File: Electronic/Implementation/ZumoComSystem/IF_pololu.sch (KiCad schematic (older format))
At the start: 38 parts, among them J4 Left, J5 Conn_02x07_Odd_Even, J6 Right, J7 Conn_02x07_Odd_Even, Q10 SI2302CDS-T1-BE3, Q6 SI2302CDS-T1-BE3, Q7 SI2302CDS-T1-BE3, Q8 SI2302CDS-T1-BE3, Q9 SI2302CDS-T1-BE3, SW3 KMR221GLFS, SW4 KMR221GLFS, SW5 KMR221GLFS

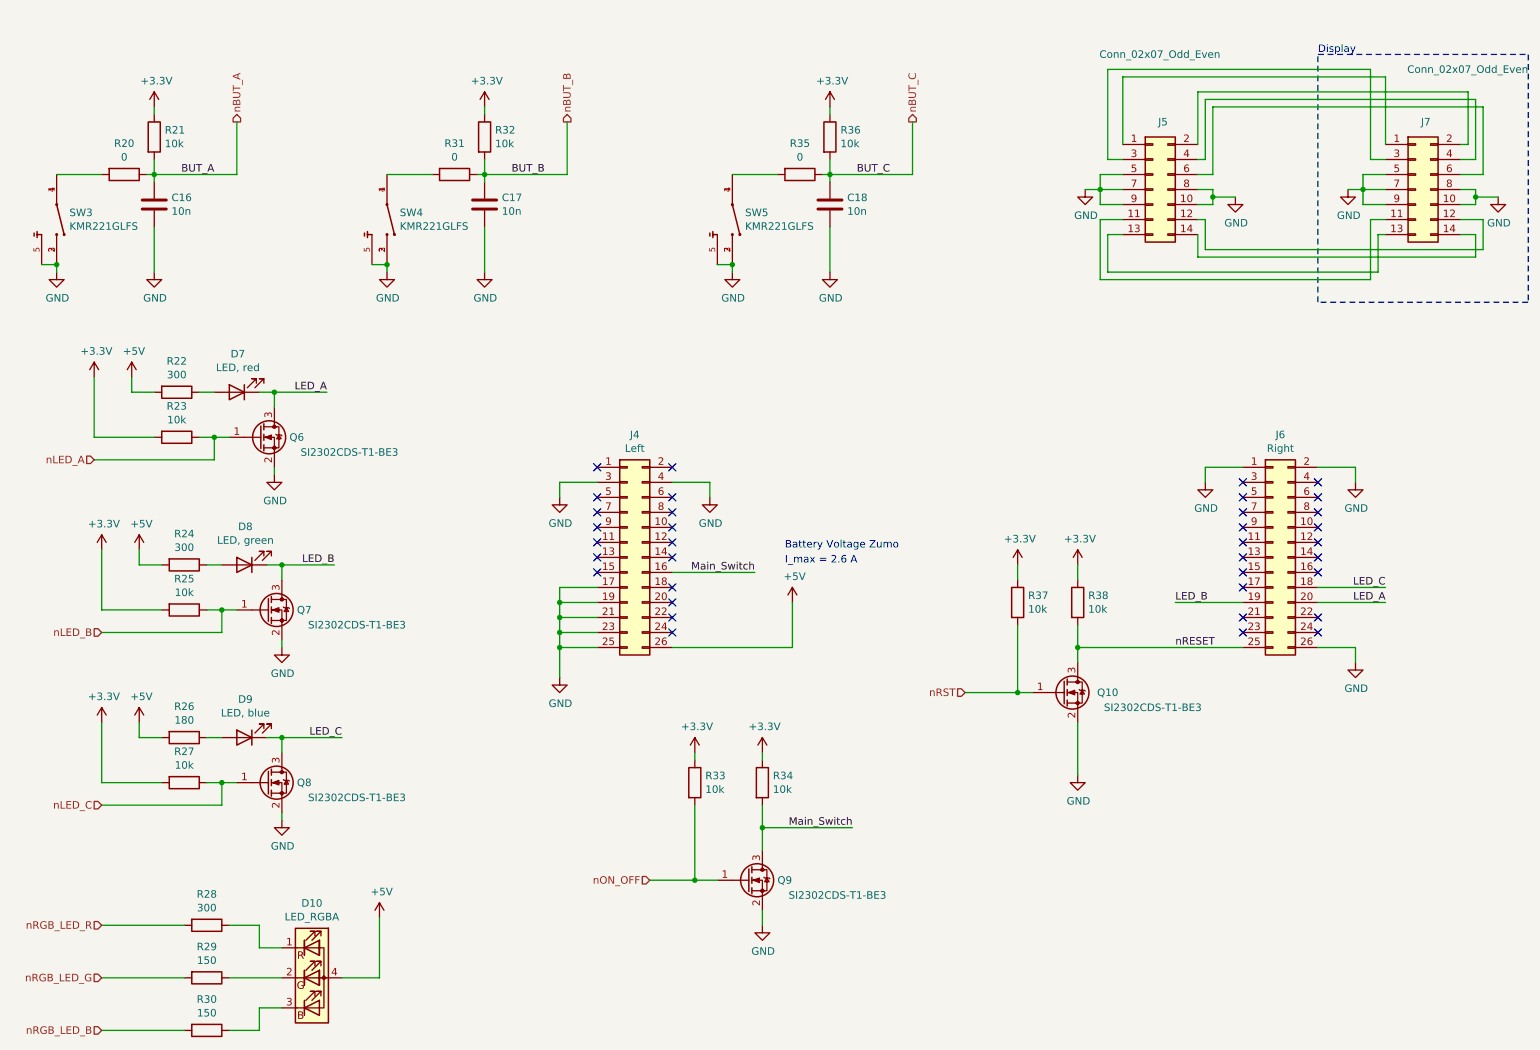
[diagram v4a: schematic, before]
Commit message: #93 ESP32 3V3 Diode; U_Bat_Meas from Pin IO2 to IO13; Test-Vias D+,D-
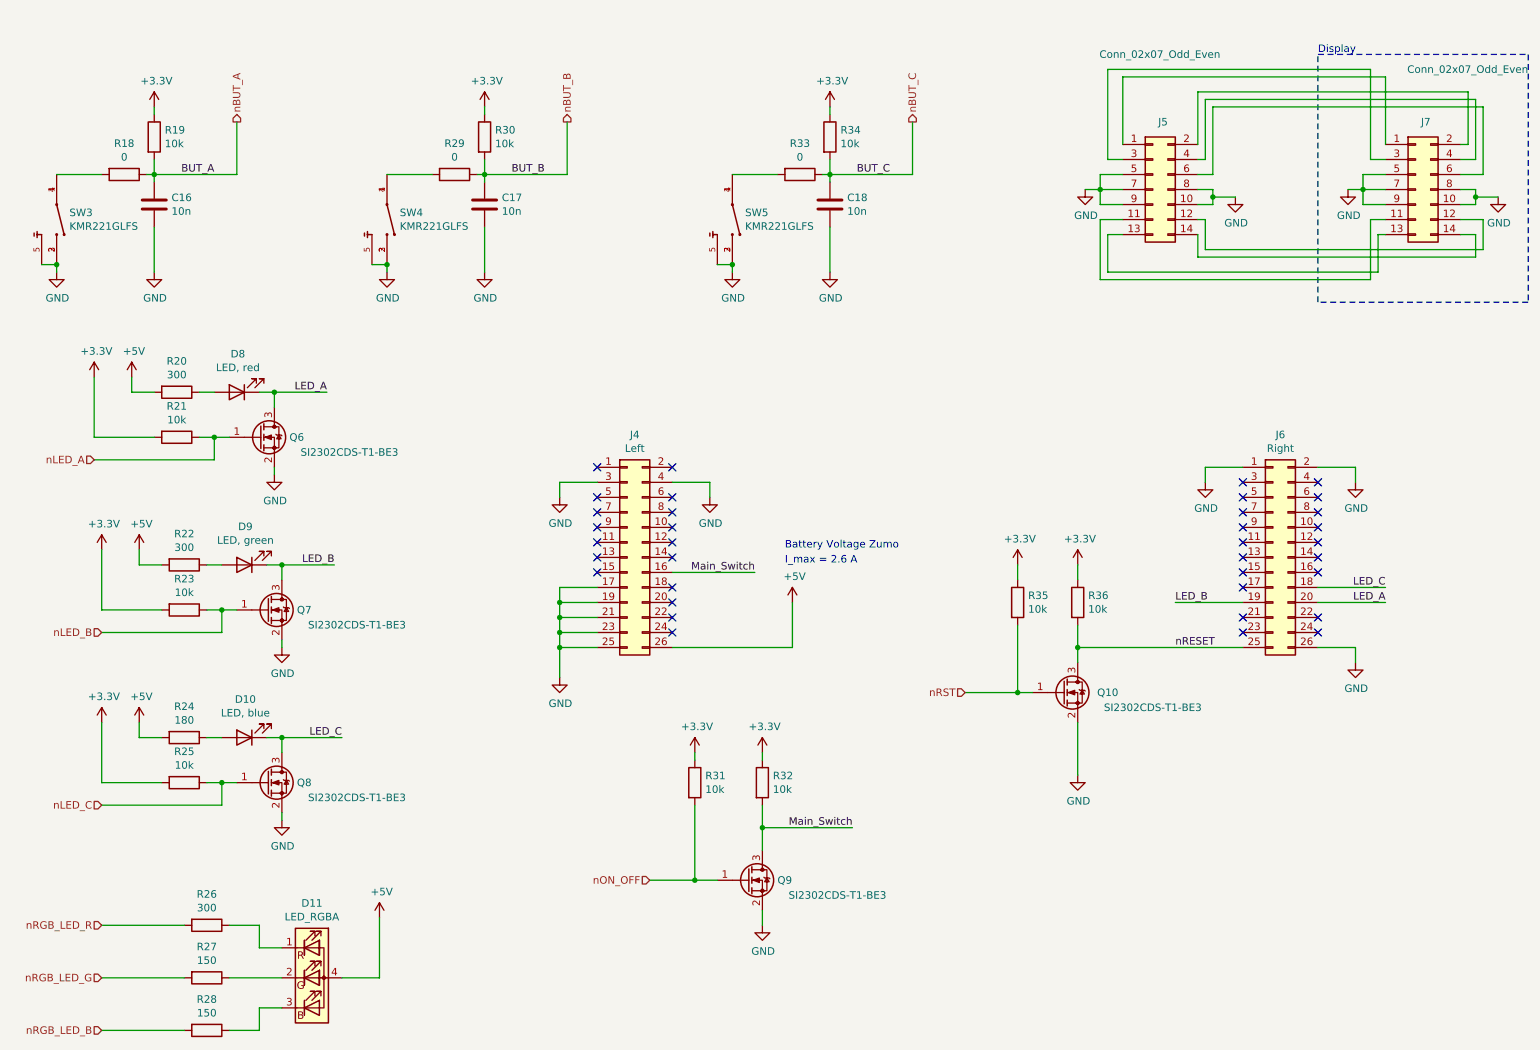
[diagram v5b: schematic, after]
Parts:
- renumbered D9 to D10, D10 to D11, D7 to D8, D8 to D9, R20 to R18, R21 to R19, R22 to R20, R23 to R21, R24 to R22, R25 to R23, R26 to R24, R27 to R25, R28 to R26, R29 to R27, R30 to R28, R31 to R29, R32 to R30, R33 to R31, R34 to R32, R35 to R33, R36 to R34, R37 to R35, R38 to R36

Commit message: #93 Peripherals RGB LED pining corrected; 0 Ohm resistors buttons remove
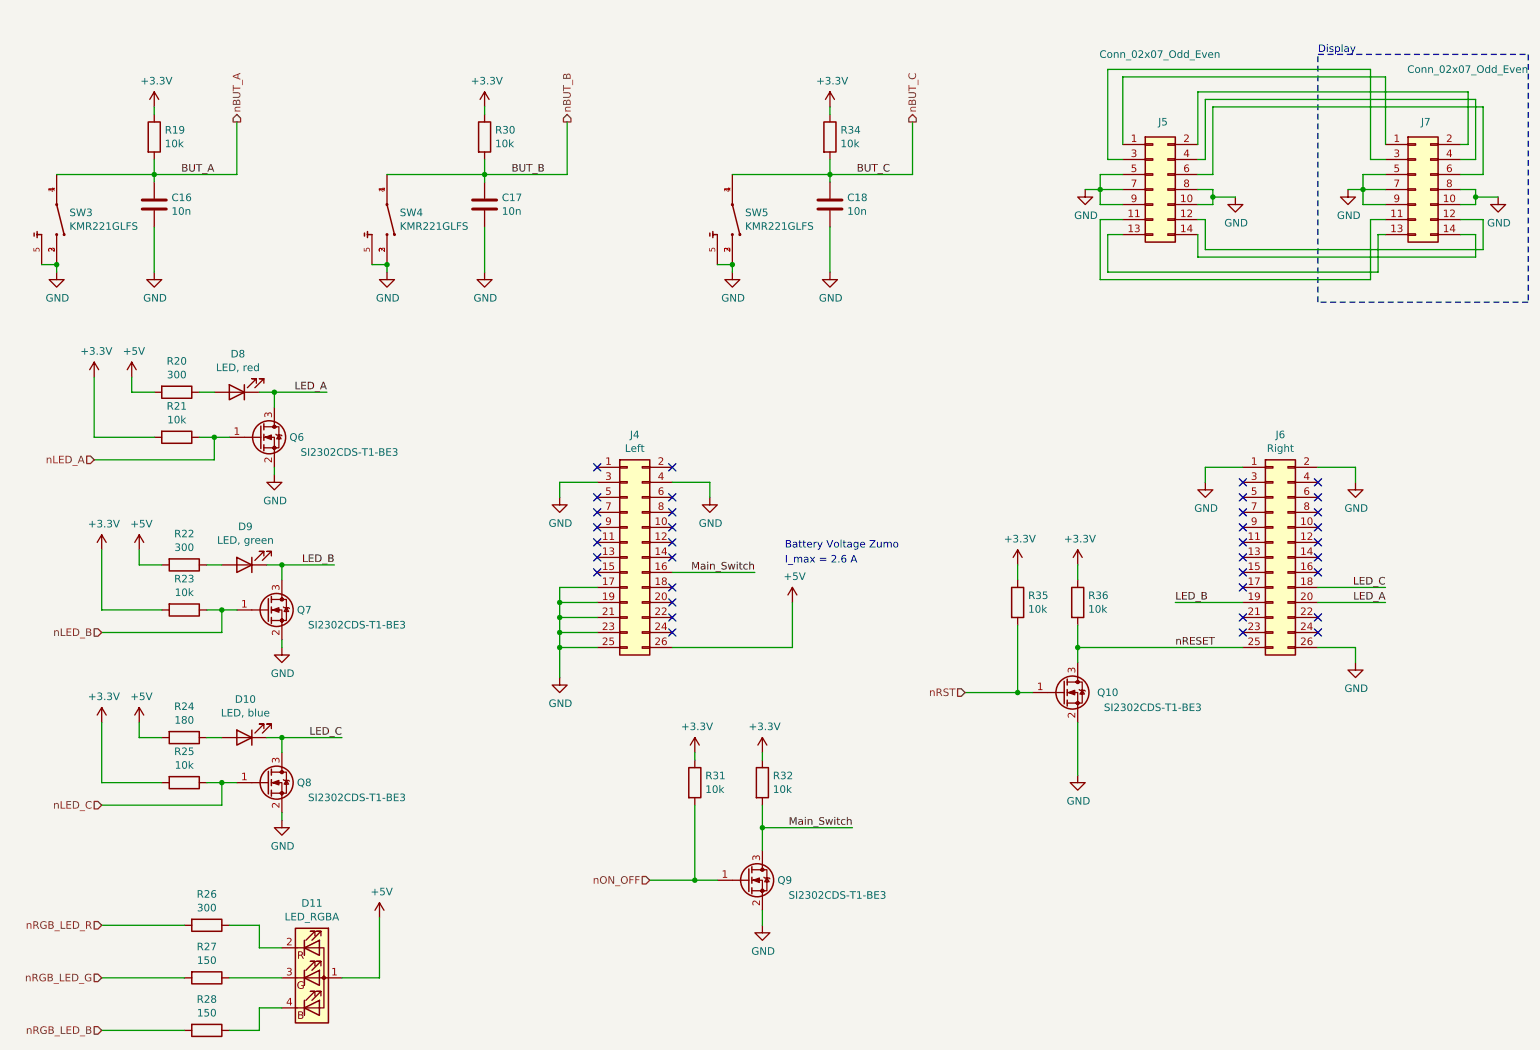
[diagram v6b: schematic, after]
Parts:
- removed D11: LED_RGBA, LED_SMD:LED_RGB_1210, symbol Device:LED_RGBA
- removed R18, R29, R33: 0, Resistor_SMD:R_0603_1608Metric_Pad1.05x0.95mm_HandSolder, symbol Device:R
- added D11: LED_RGBA, footprints:LED_RGB_1210, symbol Device:LED_ARGB
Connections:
- net +5V: now also D11.1 (A)
- net nBUT_A: now also SW3.1, SW3.4
- net nBUT_B: now also SW4.1, SW4.4
- net nBUT_C: now also SW5.1, SW5.4
- net at R26.1: now also D11.2 (RK)
- net at R27.1: now also D11.3 (GK)
- net at R28.1: now also D11.4 (BK)
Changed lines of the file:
@@
-	1    0    0    -1
-$EndComp
-$Comp
-L Device:LED_RGBA D11
-U 1 1 60FFBDC1
-P 2800 6900
-F 0 "D11" H 2800 7397 50  0000 C CNN
-F 1 "LED_RGBA" H 2800 7306 50  0000 C CNN
-F 2 "LED_SMD:LED_RGB_1210" H 2800 6850 50  0001 C CNN
-F 3 "https://docs.broadcom.com/doc/AV02-0610EN" H 2800 6850 50  0001 C CNN
-F 4 "Broadcom Limited" H 2800 6900 50  0001 C CNN "Manufacturer"
-F 5 "HSMF-C118" H 2800 6900 50  0001 C CNN "Part-No."
-	1    2800 6900
 	1    0    0    -1
 $EndComp
@@
 Wire Wire Line
 	4450 4600 4450 4500
-$Comp
-L Device:R R29
-U 1 1 617380EC
-P 3750 1550
-F 0 "R29" V 3543 1550 50  0000 C CNN
-F 1 "0" V 3634 1550 50  0000 C CNN
-F 2 "Resistor_SMD:R_0603_1608Metric_Pad1.05x0.95mm_HandSolder" V 3680 1550 50  0001 C CNN
-F 3 "~" H 3750 1550 50  0001 C CNN
-F 4 "YAGEO" H 3750 1550 50  0001 C CNN "Manufacturer"
-F 5 "RC0603FR-070RL" H 3750 1550 50  0001 C CNN "Part-No."
-	1    3750 1550
-	0    1    1    0
-$EndComp
-Wire Wire Line
-	3300 1550 3600 1550
-Wire Wire Line
-	3950 1550 3900 1550
 Connection ~ 6250 1550
-$Comp
-L Device:R R33
-U 1 1 617BFBB5
-P 6050 1550
-F 0 "R33" V 5843 1550 50  0000 C CNN
-F 1 "0" V 5934 1550 50  0000 C CNN
-F 2 "Resistor_SMD:R_0603_1608Metric_Pad1.05x0.95mm_HandSolder" V 5980 1550 50  0001 C CNN
-F 3 "~" H 6050 1550 50  0001 C CNN
-F 4 "YAGEO" H 6050 1550 50  0001 C CNN "Manufacturer"
-F 5 "RC0603FR-070RL" H 6050 1550 50  0001 C CNN "Part-No."
-	1    6050 1550
-	0    1    1    0
-$EndComp
-Wire Wire Line
-	5600 1550 5900 1550
-Wire Wire Line
-	6250 1550 6200 1550
 $Comp
 L power:GND #PWR046
@@
 	1    1100 2200
 	1    0    0    -1
-$EndComp
-$Comp
-L Device:R R18
-U 1 1 617DBB43
-P 1550 1550
-F 0 "R18" V 1343 1550 50  0000 C CNN
-F 1 "0" V 1434 1550 50  0000 C CNN
-F 2 "Resistor_SMD:R_0603_1608Metric_Pad1.05x0.95mm_HandSolder" V 1480 1550 50  0001 C CNN
-F 3 "~" H 1550 1550 50  0001 C CNN
-F 4 "YAGEO" H 1550 1550 50  0001 C CNN "Manufacturer"
-F 5 "RC0603FR-070RL" H 1550 1550 50  0001 C CNN "Part-No."
-	1    1550 1550
-	0    1    1    0
 $EndComp
 $Comp
@@
 Text Label 2150 1550 2    50   ~ 0
 BUT_A
-Wire Wire Line
-	1700 1550 1750 1550
 Connection ~ 1750 1550
 Wire Wire Line
@@
 Wire Wire Line
 	1000 2150 1100 2150
-Wire Wire Line
-	1100 1550 1400 1550
 $Comp
 L power:GND #PWR059
@@
 	1    0    0    -1
 $EndComp
+$Comp
+L Device:LED_ARGB D11
+U 1 1 62EBCED3
+P 2800 6900
+F 0 "D11" H 2800 7397 50  0000 C CNN
+F 1 "LED_RGBA" H 2800 7306 50  0000 C CNN
+F 2 "footprints:LED_RGB_1210" H 2800 6850 50  0001 C CNN
+F 3 "https://docs.broadcom.com/doc/AV02-0610EN" H 2800 6850 50  0001 C CNN
+	1    2800 6900
+	1    0    0    -1
+$EndComp
+Wire Wire Line
+	1100 1550 1750 1550
+Wire Wire Line
+	3300 1550 3950 1550
+Wire Wire Line
+	5600 1550 6250 1550
 $EndSCHEMATC

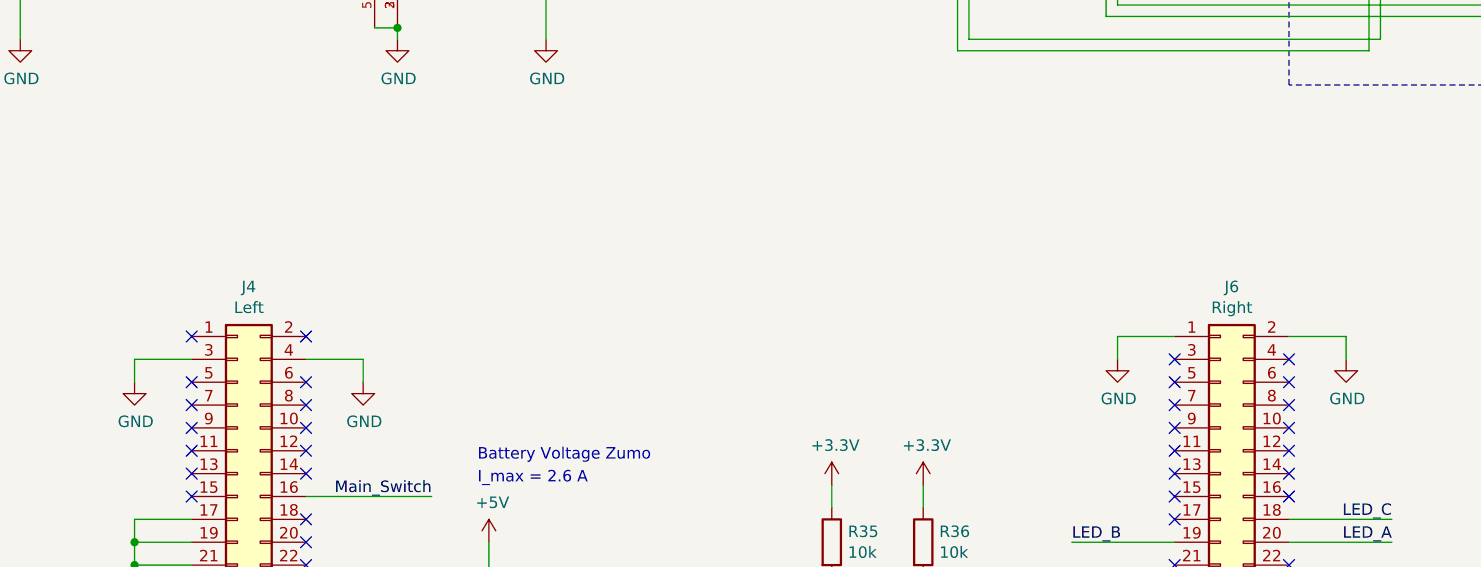
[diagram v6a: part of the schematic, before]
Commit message: Pin-Header 2x13 same value
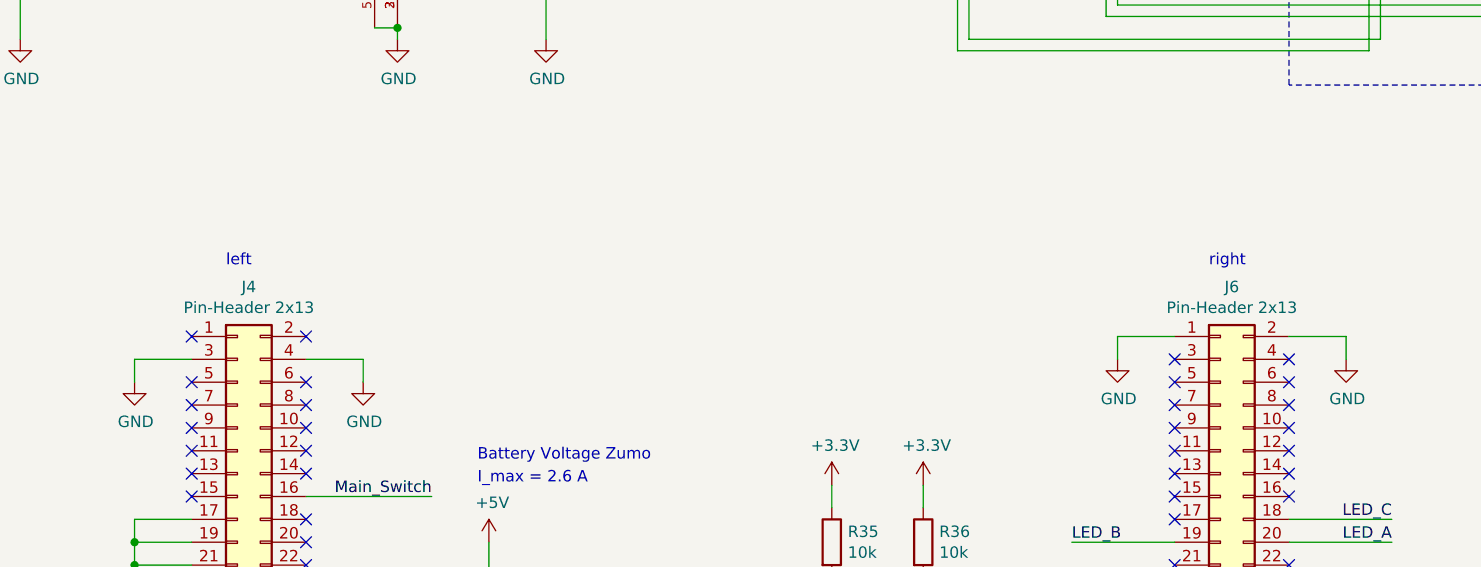
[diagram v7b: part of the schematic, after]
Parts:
- J4: value Left -> Pin-Header 2x13
- J6: value Right -> Pin-Header 2x13
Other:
- note added: "left"
- note added: "right"
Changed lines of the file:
@@
 AR Path="/60C50401/60C60623" Ref="J4"  Part="1"
 F 0 "J4" H 4950 4917 50  0000 C CNN
-F 1 "Left" H 4950 4826 50  0000 C CNN
+F 1 "Pin-Header 2x13" H 4950 4826 50  0000 C CNN
 F 2 "footprints:PinHeader_2x13_SMD_bottom" H 4900 4100 50  0001 C CNN
 F 3 "~" H 4900 4100 50  0001 C CNN
@@
 AR Path="/60C50401/60C60629" Ref="J6"  Part="1"
 F 0 "J6" H 9250 4917 50  0000 C CNN
-F 1 "Right" H 9250 4826 50  0000 C CNN
+F 1 "Pin-Header 2x13" H 9250 4826 50  0000 C CNN
 F 2 "footprints:PinHeader_2x13_SMD_bottom" H 9200 4100 50  0001 C CNN
 F 3 "~" H 9200 4100 50  0001 C CNN
@@
 Wire Wire Line
 	5600 1550 6250 1550
+Text Notes 4850 3200 0    50   ~ 0
+left
+Text Notes 9150 3200 0    50   ~ 0
+right
 $EndSCHEMATC

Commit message: Annotation update annotation
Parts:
- renumbered R19 to R20, R20 to R21, R21 to R22, R22 to R23, R23 to R24, R24 to R25, R25 to R26, R26 to R27, R27 to R28, R28 to R29, R34 to R33, R35 to R34, R36 to R35
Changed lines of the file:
@@
 nRGB_LED_B
 $Comp
-L Device:R R27
+L Device:R R28
 U 1 1 61002789
 P 2100 6900
-F 0 "R27" V 1893 6900 50  0000 C CNN
+F 0 "R28" V 1893 6900 50  0000 C CNN
 F 1 "150" V 1984 6900 50  0000 C CNN
 F 2 "Resistor_SMD:R_0603_1608Metric_Pad1.05x0.95mm_HandSolder" V 2030 6900 50  0001 C CNN
@@
 $EndComp
 $Comp
-L Device:R R28
+L Device:R R29
 U 1 1 61002936
 P 2100 7250
-F 0 "R28" V 1893 7250 50  0000 C CNN
+F 0 "R29" V 1893 7250 50  0000 C CNN
 F 1 "150" V 1984 7250 50  0000 C CNN
 F 2 "Resistor_SMD:R_0603_1608Metric_Pad1.05x0.95mm_HandSolder" V 2030 7250 50  0001 C CNN
@@
 	7900 4250 7900 4150
 $Comp
-L Device:R R36
+L Device:R R35
 U 1 1 610325C6
 P 7900 4400
-F 0 "R36" H 7970 4446 50  0000 L CNN
+F 0 "R35" H 7970 4446 50  0000 L CNN
 F 1 "10k" H 7970 4355 50  0000 L CNN
 F 2 "Resistor_SMD:R_0603_1608Metric_Pad1.05x0.95mm_HandSolder" V 7830 4400 50  0001 C CNN
@@
 	2450 3000 2550 3000
 $Comp
-L Device:R R20
+L Device:R R21
 U 1 1 617C95B1
 P 1900 3000
-F 0 "R20" V 1693 3000 50  0000 C CNN
+F 0 "R21" V 1693 3000 50  0000 C CNN
 F 1 "300" V 1784 3000 50  0000 C CNN
 F 2 "Resistor_SMD:R_0603_1608Metric_Pad1.05x0.95mm_HandSolder" V 1830 3000 50  0001 C CNN
@@
 $EndComp
 $Comp
-L Device:R R21
+L Device:R R22
 U 1 1 61109359
 P 1900 3300
-F 0 "R21" V 1693 3300 50  0000 C CNN
+F 0 "R22" V 1693 3300 50  0000 C CNN
 F 1 "10k" V 1784 3300 50  0000 C CNN
 F 2 "Resistor_SMD:R_0603_1608Metric_Pad1.05x0.95mm_HandSolder" V 1830 3300 50  0001 C CNN
@@
 	6250 1150 6250 1100
 $Comp
-L Device:R R34
+L Device:R R33
 U 1 1 613906BC
 P 6250 1300
-F 0 "R34" H 6320 1346 50  0000 L CNN
+F 0 "R33" H 6320 1346 50  0000 L CNN
 F 1 "10k" H 6320 1255 50  0000 L CNN
 F 2 "Resistor_SMD:R_0603_1608Metric_Pad1.05x0.95mm_HandSolder" V 6180 1300 50  0001 C CNN
@@
 	2500 4150 2600 4150
 $Comp
-L Device:R R22
+L Device:R R23
 U 1 1 6139F4A9
 P 1950 4150
-F 0 "R22" V 1743 4150 50  0000 C CNN
+F 0 "R23" V 1743 4150 50  0000 C CNN
 F 1 "300" V 1834 4150 50  0000 C CNN
 F 2 "Resistor_SMD:R_0603_1608Metric_Pad1.05x0.95mm_HandSolder" V 1880 4150 50  0001 C CNN
@@
 $EndComp
 $Comp
-L Device:R R23
+L Device:R R24
 U 1 1 6139F4C7
 P 1950 4450
-F 0 "R23" V 1743 4450 50  0000 C CNN
+F 0 "R24" V 1743 4450 50  0000 C CNN
 F 1 "10k" V 1834 4450 50  0000 C CNN
 F 2 "Resistor_SMD:R_0603_1608Metric_Pad1.05x0.95mm_HandSolder" V 1880 4450 50  0001 C CNN
@@
 	2500 5300 2600 5300
 $Comp
-L Device:R R24
+L Device:R R25
 U 1 1 618039F3
 P 1950 5300
-F 0 "R24" V 1743 5300 50  0000 C CNN
+F 0 "R25" V 1743 5300 50  0000 C CNN
 F 1 "180" V 1834 5300 50  0000 C CNN
 F 2 "Resistor_SMD:R_0603_1608Metric_Pad1.05x0.95mm_HandSolder" V 1880 5300 50  0001 C CNN
@@
 	7500 4250 7500 4150
 $Comp
-L Device:R R35
+L Device:R R34
 U 1 1 6196F511
 P 7500 4400
-F 0 "R35" H 7570 4446 50  0000 L CNN
+F 0 "R34" H 7570 4446 50  0000 L CNN
 F 1 "10k" H 7570 4355 50  0000 L CNN
 F 2 "Resistor_SMD:R_0603_1608Metric_Pad1.05x0.95mm_HandSolder" V 7430 4400 50  0001 C CNN
@@
 	1400 5600 1800 5600
 $Comp
-L Device:R R25
+L Device:R R26
 U 1 1 61803A11
 P 1950 5600
-F 0 "R25" V 1743 5600 50  0000 C CNN
+F 0 "R26" V 1743 5600 50  0000 C CNN
 F 1 "10k" V 1834 5600 50  0000 C CNN
 F 2 "Resistor_SMD:R_0603_1608Metric_Pad1.05x0.95mm_HandSolder" V 1880 5600 50  0001 C CNN
@@
 	2250 6900 2600 6900
 $Comp
-L Device:R R26
+L Device:R R27
 U 1 1 61001F8A
 P 2100 6550
-F 0 "R26" V 1893 6550 50  0000 C CNN
+F 0 "R27" V 1893 6550 50  0000 C CNN
 F 1 "300" V 1984 6550 50  0000 C CNN
 F 2 "Resistor_SMD:R_0603_1608Metric_Pad1.05x0.95mm_HandSolder" V 2030 6550 50  0001 C CNN
@@
 	1750 1450 1750 1550
 $Comp
-L Device:R R19
+L Device:R R20
 U 1 1 612AF006
 P 1750 1300
-F 0 "R19" H 1820 1346 50  0000 L CNN
+F 0 "R20" H 1820 1346 50  0000 L CNN
 F 1 "10k" H 1820 1255 50  0000 L CNN
 F 2 "Resistor_SMD:R_0603_1608Metric_Pad1.05x0.95mm_HandSolder" V 1680 1300 50  0001 C CNN
